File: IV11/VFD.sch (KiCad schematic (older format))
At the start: 63 parts, among them J1 USB_B, SW1 switch, SW2 switch, SW3 switch, SW4 switch, U1 74HC595, U10 UDN2981, U11 UDN2981, U12 UDN2981, U13 WeMos_mini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

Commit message: Change LDR resistor val to 22k
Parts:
- R5: value 100k -> 22k
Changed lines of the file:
@@
 P 7350 8400
 F 0 "R5" H 7420 8446 50  0000 L CNN
-F 1 "100k" H 7420 8355 50  0000 L CNN
+F 1 "22k" H 7420 8355 50  0000 L CNN
 F 2 "Resistor_THT:R_Axial_DIN0411_L9.9mm_D3.6mm_P12.70mm_Horizontal" V 7280 8400 50  0001 C CNN
 F 3 "~" H 7350 8400 50  0001 C CNN

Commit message: Final updates to complete PCB revision 1.2 including an I2C breakout connector
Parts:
- removed U21: DS18B20, Connector_PinHeader_2.54mm:PinHeader_1x03_P2.54mm_Vertical, symbol Sensor_Temperature:DS18B20
- added J2: I2C_CONN, Connector_PinHeader_2.54mm:PinHeader_1x04_P2.54mm_Horizontal, symbol Connector_Generic:Conn_01x04
- U18: symbol GenericModules:MP2307BuckConverterModule -> VFD-rescue:MP2307BuckConverterModule-GenericModules
- U19: symbol GenericModules:MT3608BoostConverterModule -> VFD-rescue:MT3608BoostConverterModule-GenericModules
- U20: symbol GenericModules:DS3231RTCModule -> VFD-rescue:DS3231RTCModule-GenericModules
- VFD1, VFD2, VFD3, VFD4, VFD5, VFD6, VFD7, VFD8: symbol vfd:IV-11 -> VFD-rescue:IV-11-vfd
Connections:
- wire segments 600 -> 605
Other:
- note removed: "Optional DS18B20\ninstead of SW1"
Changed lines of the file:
@@
 	4550 1250 4750 1250
 $Comp
-L vfd:IV-11 VFD1
+L VFD-rescue:IV-11-vfd VFD1
 U 1 1 5B727BC1
 P 4200 2000
@@
 	4550 3550 4750 3550
 $Comp
-L vfd:IV-11 VFD3
+L VFD-rescue:IV-11-vfd VFD3
 U 1 1 5B72D955
 P 4200 4300
@@
 	4550 5900 4750 5900
 $Comp
-L vfd:IV-11 VFD5
+L VFD-rescue:IV-11-vfd VFD5
 U 1 1 5B7320B7
 P 4200 6650
@@
 	9500 1450 9700 1450
 $Comp
-L vfd:IV-11 VFD2
+L VFD-rescue:IV-11-vfd VFD2
 U 1 1 5B73C1FB
 P 9150 2200
@@
 	9500 3750 9700 3750
 $Comp
-L vfd:IV-11 VFD4
+L VFD-rescue:IV-11-vfd VFD4
 U 1 1 5B74BC81
 P 9150 4500
@@
 	9500 5950 9700 5950
 $Comp
-L vfd:IV-11 VFD6
+L VFD-rescue:IV-11-vfd VFD6
 U 1 1 5B76357F
 P 9150 6700
@@
 	14350 1650 14550 1650
 $Comp
-L vfd:IV-11 VFD7
+L VFD-rescue:IV-11-vfd VFD7
 U 1 1 5B4DE300
 P 14000 2400
@@
 	14350 3850 14550 3850
 $Comp
-L vfd:IV-11 VFD8
+L VFD-rescue:IV-11-vfd VFD8
 U 1 1 5B5EC07F
 P 14000 4600
@@
 $EndComp
 $Comp
-L GenericModules:MP2307BuckConverterModule U18
+L VFD-rescue:MP2307BuckConverterModule-GenericModules U18
 U 1 1 5B8B2710
 P 12500 8850
@@
 	13050 8350 13050 8650
 $Comp
-L GenericModules:MT3608BoostConverterModule U19
+L VFD-rescue:MT3608BoostConverterModule-GenericModules U19
 U 1 1 5BAFC179
 P 14050 8750
@@
 	1000 9750 1000 10750
 $Comp
-L GenericModules:DS3231RTCModule U20
+L VFD-rescue:DS3231RTCModule-GenericModules U20
 U 1 1 5BDC61FB
 P 4150 9700
@@
 Wire Wire Line
 	7900 9350 7900 9950
-$Comp
-L Sensor_Temperature:DS18B20 U21
-U 1 1 5B70AEE5
-P 11250 6100
-F 0 "U21" H 11020 6146 50  0000 R CNN
-F 1 "DS18B20" H 11020 6055 50  0000 R CNN
-F 2 "Connector_PinHeader_2.54mm:PinHeader_1x03_P2.54mm_Vertical" H 10250 5850 50  0001 C CNN
-F 3 "http://datasheets.maximintegrated.com/en/ds/DS18B20.pdf" H 11100 6350 50  0001 C CNN
-	1    11250 6100
-	1    0    0    -1
-$EndComp
 Wire Wire Line
 	8650 6050 8650 6200
 Wire Wire Line
 	8650 3850 8650 4000
-$Comp
-L power:GND #PWR0207
-U 1 1 5B7663A8
-P 11250 6400
-F 0 "#PWR0207" H 11250 6150 50  0001 C CNN
-F 1 "GND" H 11255 6227 50  0000 C CNN
-F 2 "" H 11250 6400 50  0001 C CNN
-F 3 "" H 11250 6400 50  0001 C CNN
-	1    11250 6400
-	1    0    0    -1
-$EndComp
-$Comp
-L power:+3V3 #PWR0208
-U 1 1 5B76650C
-P 11250 5800
-F 0 "#PWR0208" H 11250 5650 50  0001 C CNN
-F 1 "+3V3" H 11265 5973 50  0000 C CNN
-F 2 "" H 11250 5800 50  0001 C CNN
-F 3 "" H 11250 5800 50  0001 C CNN
-	1    11250 5800
-	1    0    0    -1
-$EndComp
-Text GLabel 11550 6100 2    50   Input ~ 0
-SW_1
-Text Notes 12000 5850 2    50   ~ 0
-Optional DS18B20\ninstead of SW1
 Wire Wire Line
 	7150 9150 7150 9350
@@
 	7150 9850 7150 10050
 Connection ~ 7150 9850
+$Comp
+L Connector_Generic:Conn_01x04 J2
+U 1 1 5BFB814D
+P 11450 6150
+F 0 "J2" H 11530 6142 50  0000 L CNN
+F 1 "I2C_CONN" H 11530 6051 50  0000 L CNN
+F 2 "Connector_PinHeader_2.54mm:PinHeader_1x04_P2.54mm_Horizontal" H 11450 6150 50  0001 C CNN
+F 3 "~" H 11450 6150 50  0001 C CNN
+	1    11450 6150
+	1    0    0    -1
+$EndComp
+Wire Wire Line
+	11250 6050 11000 6050
+Wire Wire Line
+	11250 6150 11000 6150
+Wire Wire Line
+	11250 6350 11000 6350
+$Comp
+L power:+3V3 #PWR0207
+U 1 1 5C175A14
+P 11000 6050
+F 0 "#PWR0207" H 11000 5900 50  0001 C CNN
+F 1 "+3V3" H 11015 6223 50  0000 C CNN
+F 2 "" H 11000 6050 50  0001 C CNN
+F 3 "" H 11000 6050 50  0001 C CNN
+	1    11000 6050
+	1    0    0    -1
+$EndComp
+Wire Wire Line
+	10800 6250 10800 6450
+Wire Wire Line
+	10800 6250 11250 6250
+$Comp
+L power:GND #PWR0208
+U 1 1 5C1D00BB
+P 10800 6450
+F 0 "#PWR0208" H 10800 6200 50  0001 C CNN
+F 1 "GND" H 10805 6277 50  0000 C CNN
+F 2 "" H 10800 6450 50  0001 C CNN
+F 3 "" H 10800 6450 50  0001 C CNN
+	1    10800 6450
+	1    0    0    -1
+$EndComp
+Text GLabel 11000 6150 0    50   Input ~ 0
+SDA
+Text GLabel 11000 6350 0    50   Input ~ 0
+SCL
 $EndSCHEMATC

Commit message: Major redesign to use different buck converter, and also up-rate track thickness for power rails
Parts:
- removed U18: MiniBuckBoard, GenericModules:MP2307BuckConverterModule, symbol VFD-rescue:MP2307BuckConverterModule-GenericModules
- added U18: LM2596BuckConverterModule, GenericModules:LM2596BuckConverterModule, symbol GenericModules:LM2596BuckConverterModule
- D1, D2, D3, D4, D5, D6, D7, D8: symbol 5mmNeopixel:NeoPixel_THT -> VFD-rescue:NeoPixel_THT-5mmNeopixel
- U10, U11, U12, U16, U17, U4, U5, U6: symbol UDN2981-THT:UDN2981-THT -> VFD-rescue:UDN2981-THT-UDN2981-THT
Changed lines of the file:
@@
 EESchema Schematic File Version 4
 LIBS:VFD-cache
-EELAYER 26 0
+EELAYER 30 0
 EELAYER END
 $Descr A3 16535 11693
@@
 $EndDescr
 $Comp
-L UDN2981-THT:UDN2981-THT U4
+L VFD-rescue:UDN2981-THT-UDN2981-THT U4
 U 1 1 5B727B46
 P 3150 1800
@@
 TUBE_1_DATA_OUT
 $Comp
-L UDN2981-THT:UDN2981-THT U5
+L VFD-rescue:UDN2981-THT-UDN2981-THT U5
 U 1 1 5B72D8DA
 P 3150 4100
@@
 TUBE_3_DATA_OUT
 $Comp
-L UDN2981-THT:UDN2981-THT U6
+L VFD-rescue:UDN2981-THT-UDN2981-THT U6
 U 1 1 5B73203C
 P 3150 6450
@@
 TUBE_5_DATA_OUT
 $Comp
-L UDN2981-THT:UDN2981-THT U10
+L VFD-rescue:UDN2981-THT-UDN2981-THT U10
 U 1 1 5B73C180
 P 8100 2000
@@
 TUBE_2_DATA_OUT
 $Comp
-L UDN2981-THT:UDN2981-THT U11
+L VFD-rescue:UDN2981-THT-UDN2981-THT U11
 U 1 1 5B74BC06
 P 8100 4300
@@
 TUBE_4_DATA_OUT
 $Comp
-L UDN2981-THT:UDN2981-THT U12
+L VFD-rescue:UDN2981-THT-UDN2981-THT U12
 U 1 1 5B763504
 P 8100 6500
@@
 $EndComp
 $Comp
-L UDN2981-THT:UDN2981-THT U16
+L VFD-rescue:UDN2981-THT-UDN2981-THT U16
 U 1 1 5B4DE28E
 P 12950 2200
@@
 $EndComp
 $Comp
-L UDN2981-THT:UDN2981-THT U17
+L VFD-rescue:UDN2981-THT-UDN2981-THT U17
 U 1 1 5B5EC00E
 P 12950 4400
@@
 L power:+1V5 #PWR0145
 U 1 1 5B6ECA8F
-P 12050 8350
-F 0 "#PWR0145" H 12050 8200 50  0001 C CNN
-F 1 "+1V5" H 12065 8523 50  0000 C CNN
-F 2 "" H 12050 8350 50  0001 C CNN
-F 3 "" H 12050 8350 50  0001 C CNN
-	1    12050 8350
-	1    0    0    -1
-$EndComp
-$Comp
-L VFD-rescue:MP2307BuckConverterModule-GenericModules U18
-U 1 1 5B8B2710
-P 12500 8850
-F 0 "U18" H 12550 9315 50  0000 C CNN
-F 1 "MiniBuckBoard" H 12550 9224 50  0000 C CNN
-F 2 "GenericModules:MP2307BuckConverterModule" H 12500 8850 50  0001 C CNN
-F 3 "" H 12500 8850 50  0001 C CNN
-	1    12500 8850
+P 13050 8350
+F 0 "#PWR0145" H 13050 8200 50  0001 C CNN
+F 1 "+1V5" H 13065 8523 50  0000 C CNN
+F 2 "" H 13050 8350 50  0001 C CNN
+F 3 "" H 13050 8350 50  0001 C CNN
+	1    13050 8350
 	1    0    0    -1
 $EndComp
-Wire Wire Line
-	13050 8950 13050 9200
-Wire Wire Line
-	12050 8950 12050 9200
 $Comp
 L power:+5V #PWR0153
 U 1 1 5B976A52
-P 13050 8350
-F 0 "#PWR0153" H 13050 8200 50  0001 C CNN
-F 1 "+5V" H 13065 8523 50  0000 C CNN
-F 2 "" H 13050 8350 50  0001 C CNN
-F 3 "" H 13050 8350 50  0001 C CNN
-	1    13050 8350
+P 12050 8350
+F 0 "#PWR0153" H 12050 8200 50  0001 C CNN
+F 1 "+5V" H 12065 8523 50  0000 C CNN
+F 2 "" H 12050 8350 50  0001 C CNN
+F 3 "" H 12050 8350 50  0001 C CNN
+	1    12050 8350
 	1    0    0    -1
 $EndComp
@@
 	14000 5500 14700 5500
 $Comp
-L 5mmNeopixel:NeoPixel_THT D6
+L VFD-rescue:NeoPixel_THT-5mmNeopixel D6
 U 1 1 5C6047BD
 P 9750 9600
@@
 $EndComp
 $Comp
-L 5mmNeopixel:NeoPixel_THT D3
+L VFD-rescue:NeoPixel_THT-5mmNeopixel D3
 U 1 1 5C64AD7C
 P 10400 8650
@@
 $EndComp
 $Comp
-L 5mmNeopixel:NeoPixel_THT D5
+L VFD-rescue:NeoPixel_THT-5mmNeopixel D5
 U 1 1 5C64AE2E
 P 9100 9600
@@
 $EndComp
 $Comp
-L 5mmNeopixel:NeoPixel_THT D2
+L VFD-rescue:NeoPixel_THT-5mmNeopixel D2
 U 1 1 5C64AEE3
 P 9750 8650
@@
 $EndComp
 $Comp
-L 5mmNeopixel:NeoPixel_THT D7
+L VFD-rescue:NeoPixel_THT-5mmNeopixel D7
 U 1 1 5C64B041
 P 10400 9600
@@
 $EndComp
 $Comp
-L 5mmNeopixel:NeoPixel_THT D8
+L VFD-rescue:NeoPixel_THT-5mmNeopixel D8
 U 1 1 5C64B128
 P 11050 9600
@@
 $EndComp
 $Comp
-L 5mmNeopixel:NeoPixel_THT D4
+L VFD-rescue:NeoPixel_THT-5mmNeopixel D4
 U 1 1 5C64B206
 P 11100 8650
@@
 	9750 8950 10400 8950
 $Comp
-L 5mmNeopixel:NeoPixel_THT D1
+L VFD-rescue:NeoPixel_THT-5mmNeopixel D1
 U 1 1 5C64AC77
 P 9100 8650
@@
 Text GLabel 11000 6350 0    50   Input ~ 0
 SCL
+$Comp
+L GenericModules:LM2596BuckConverterModule U18
+U 1 1 5DD10807
+P 12500 8850
+F 0 "U18" H 12550 9315 50  0000 C CNN
+F 1 "LM2596BuckConverterModule" H 12550 9224 50  0000 C CNN
+F 2 "GenericModules:LM2596BuckConverterModule" H 12600 9300 50  0001 C CNN
+F 3 "" H 12500 8850 50  0001 C CNN
+	1    12500 8850
+	1    0    0    -1
+$EndComp
+Wire Wire Line
+	13050 8950 13050 9200
+Wire Wire Line
+	12050 8950 12050 9200
 $EndSCHEMATC

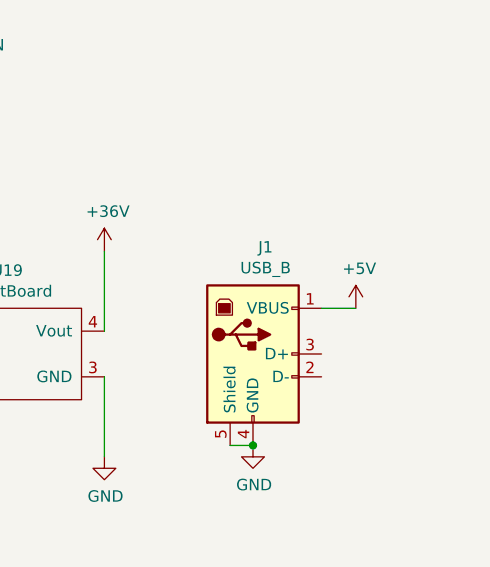
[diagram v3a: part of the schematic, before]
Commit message: Add in room for polyfuse
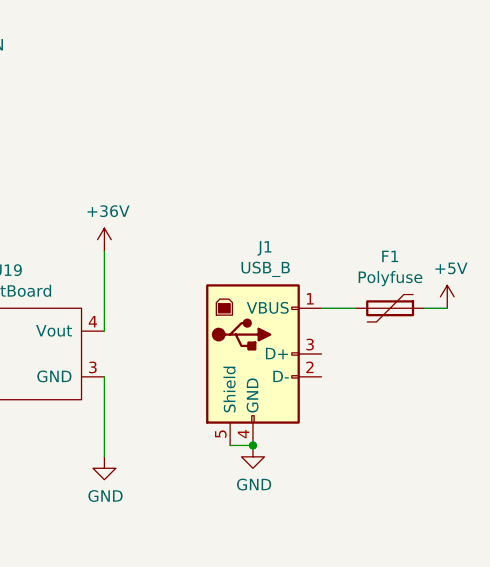
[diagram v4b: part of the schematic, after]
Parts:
- added F1: Polyfuse, Resistor_THT:R_Axial_DIN0309_L9.0mm_D3.2mm_P15.24mm_Horizontal, symbol Device:Polyfuse
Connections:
- net +5V: now also F1.1; no longer J1.1 (VBUS)
- new net: F1.2, J1.1 (VBUS)
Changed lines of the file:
@@
 L power:+5V #PWR0177
 U 1 1 5BC81A8E
-P 15600 8550
-F 0 "#PWR0177" H 15600 8400 50  0001 C CNN
-F 1 "+5V" H 15615 8723 50  0000 C CNN
-F 2 "" H 15600 8550 50  0001 C CNN
-F 3 "" H 15600 8550 50  0001 C CNN
-	1    15600 8550
+P 16000 8550
+F 0 "#PWR0177" H 16000 8400 50  0001 C CNN
+F 1 "+5V" H 16015 8723 50  0000 C CNN
+F 2 "" H 16000 8550 50  0001 C CNN
+F 3 "" H 16000 8550 50  0001 C CNN
+	1    16000 8550
 	1    0    0    -1
 $EndComp
@@
 Wire Wire Line
 	12050 8950 12050 9200
+$Comp
+L Device:Polyfuse F1
+U 1 1 5DD1DD97
+P 15750 8550
+F 0 "F1" V 15525 8550 50  0000 C CNN
+F 1 "Polyfuse" V 15616 8550 50  0000 C CNN
+F 2 "Resistor_THT:R_Axial_DIN0309_L9.0mm_D3.2mm_P15.24mm_Horizontal" H 15800 8350 50  0001 L CNN
+F 3 "~" H 15750 8550 50  0001 C CNN
+	1    15750 8550
+	0    1    1    0
+$EndComp
+Wire Wire Line
+	15900 8550 16000 8550
 $EndSCHEMATC

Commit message: Update thickness of 48VDC tracks x
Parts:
- U18: symbol GenericModules:LM2596BuckConverterModule -> VFD-rescue:LM2596BuckConverterModule-GenericModules
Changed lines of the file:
@@
 SCL
 $Comp
-L GenericModules:LM2596BuckConverterModule U18
+L VFD-rescue:LM2596BuckConverterModule-GenericModules U18
 U 1 1 5DD10807
 P 12500 8850
